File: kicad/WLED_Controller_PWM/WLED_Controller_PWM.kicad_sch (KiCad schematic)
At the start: 45 parts, among them J1 USB_C_Receptacle_USB2.0, J2 Conn_01x03, J3 Conn_01x03, J4 Conn_01x03, J6 Conn_01x02, Q1 BC847, Q2 BC847, SW1 SW_RESET, SW2 SW_BOOT, SW3 SW_Push, U1 ESP32-WROOM-32, U2 CH340C, U3 NCP1117-3.3, U4 TSSP58P38, U5 74HC14

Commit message: Add PWM Controllers
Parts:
- removed C13: 100n, Capacitor_SMD:C_0603_1608Metric_Pad1.08x0.95mm_HandSolder, symbol Device:C
- removed J2, J3, J4: Conn_01x03, GioN_Custom:TerminalBlock_WAGO_236-403_1x03_P5.00mm_45Degree, symbol Connector_Generic:Conn_01x03
- removed U5: 74HC14, Package_SO:SOIC-14_3.9x8.7mm_P1.27mm, symbol 74xx:74HC14
- added J5: Conn_01x05, GioN_Custom:TerminalBlock_WAGO_236-405_1x05_P5.00mm_45Degree, symbol Connector_Generic:Conn_01x05
- added Q3, Q4, Q5, Q6: IRFL4105PBF, Package_TO_SOT_SMD:SOT-223, symbol Transistor_FET:IRF540N
- added R13, R15, R17, R19: 100R, Resistor_SMD:R_0603_1608Metric_Pad0.98x0.95mm_HandSolder, symbol Device:R
- added R14, R16, R18, R20: 10k, Resistor_SMD:R_0603_1608Metric_Pad0.98x0.95mm_HandSolder, symbol Device:R
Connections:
- net +5V: no longer J6.1 (Pin_1)
- net GND: now also Q3.3 (S), Q4.3 (S), Q5.3 (S), Q6.3 (S), R14.1, R16.1, R18.1, R20.1
- net IO18 renamed LED_W
- net LED_W: now also R19.1
- net LED0 renamed LED_R
- net LED_R: now also R13.1
- net LED1 renamed LED_G
- net LED_G: now also R15.1
- net LED2 renamed LED_B
- net LED_B: now also R17.1
- new net: Q4.1 (G), R15.2, R16.2
- new net: Q6.1 (G), R19.2, R20.2
- new net: Q3.1 (G), R13.2, R14.2
- new net: Q5.1 (G), R17.2, R18.2
- new net: J5.4 (Pin_4), Q5.2 (D)
- new net: J5.5 (Pin_5), Q6.2 (D)
- new net: J5.2 (Pin_2), Q3.2 (D)
- new net: J5.3 (Pin_3), Q4.2 (D)
- new net +12V: J5.1 (Pin_1), J6.1 (Pin_1)

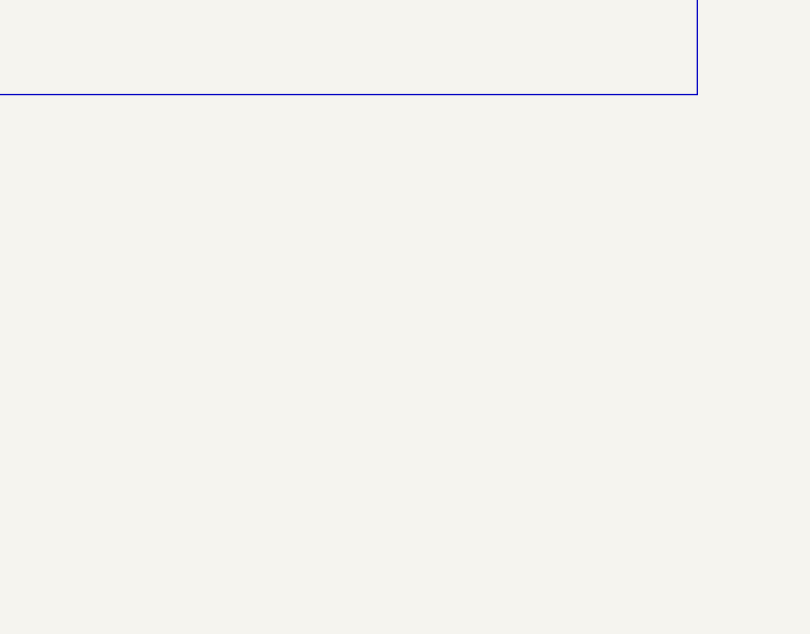
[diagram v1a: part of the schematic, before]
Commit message: add 7805
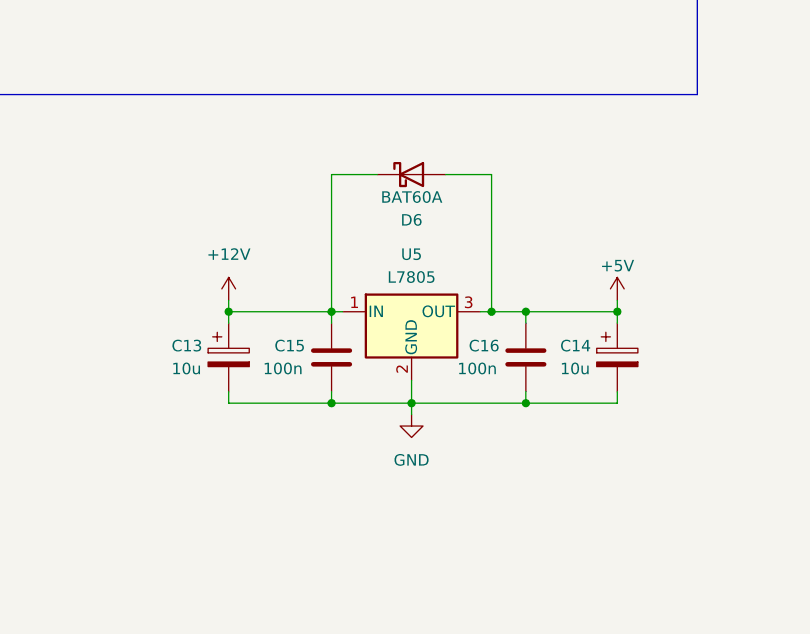
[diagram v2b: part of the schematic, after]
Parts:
- added C13, C14: 10u, Capacitor_Tantalum_SMD:CP_EIA-3216-18_Kemet-A_Pad1.58x1.35mm_HandSolder, symbol Device:C_Polarized
- added C15, C16: 100n, Capacitor_SMD:C_0603_1608Metric_Pad1.08x0.95mm_HandSolder, symbol Device:C
- added D6: BAT60A, Diode_SMD:D_SOD-323_HandSoldering, symbol Diode:BAT60A
- added U5: L7805, Package_TO_SOT_SMD:TO-252-3_TabPin2, symbol Regulator_Linear:L7805
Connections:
- net +12V: now also C13.1, C15.1, D6.1 (K), U5.1 (IN)
- net +5V: now also C14.1, C16.1, D6.2 (A), U5.3 (OUT)
- net GND: now also C13.2, C14.2, C15.2, C16.2, U5.2 (GND)

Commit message: Change to WAGO250
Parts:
- J5: footprint GioN_Custom:TerminalBlock_WAGO_236-405_1x05_P5.00mm_45Degree -> GioN_Custom:WAGO_250-205_1x05_P3.50mm
- J6: footprint GioN_Custom:TerminalBlock_WAGO_236-402_1x02_P5.00mm_45Degree -> GioN_Custom:WAGO_250-202_1x02_P3.50mm
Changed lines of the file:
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@@
       (effects (font (size 1.27 1.27)) (justify left))
     )
-    (property "Footprint" "GioN_Custom:TerminalBlock_WAGO_236-405_1x05_P5.00mm_45Degree" (at 444.5 124.46 0)
+    (property "Footprint" "GioN_Custom:WAGO_250-205_1x05_P3.50mm" (at 444.5 124.46 0)
       (effects (font (size 1.27 1.27)) hide)
     )
@@
       (effects (font (size 1.27 1.27)) (justify left))
     )
-    (property "Footprint" "GioN_Custom:TerminalBlock_WAGO_236-402_1x02_P5.00mm_45Degree" (at 125.73 134.62 0)
-      (effects (font (size 1.27 1.27)) hide)
-    )
+    (property "Footprint" "GioN_Custom:WAGO_250-202_1x02_P3.50mm" (at 125.73 134.62 0)
+      (effects (font (size 1.27 1.27)) hide)
+    )

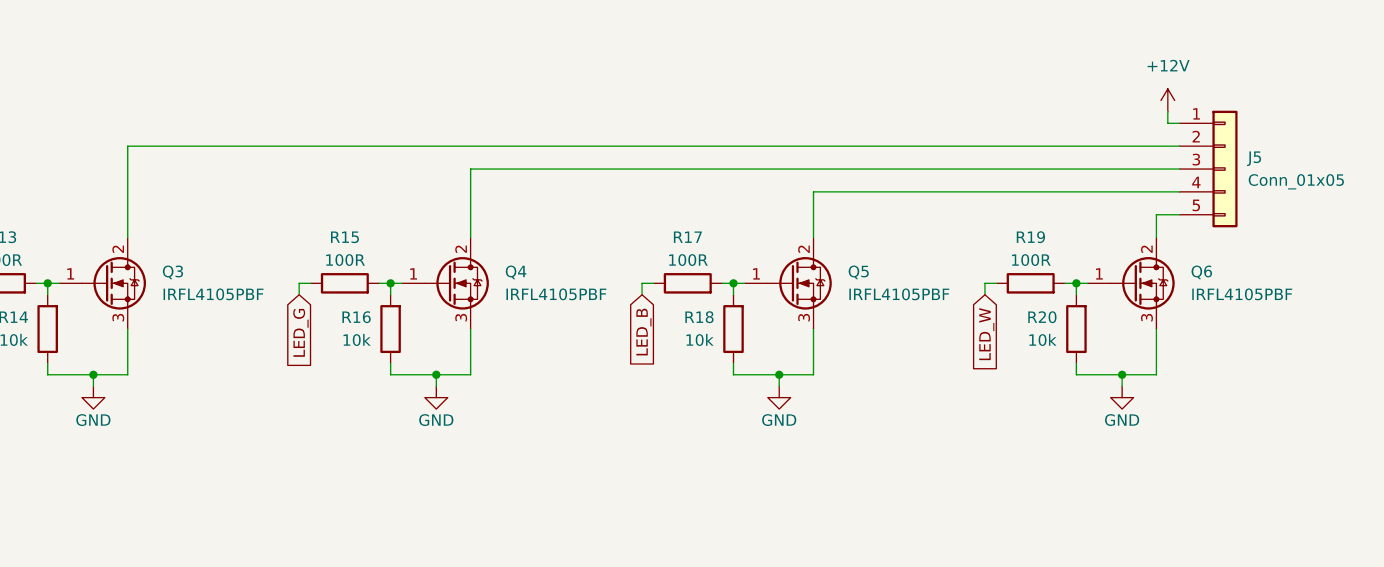
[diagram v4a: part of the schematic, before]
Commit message: change mosfet
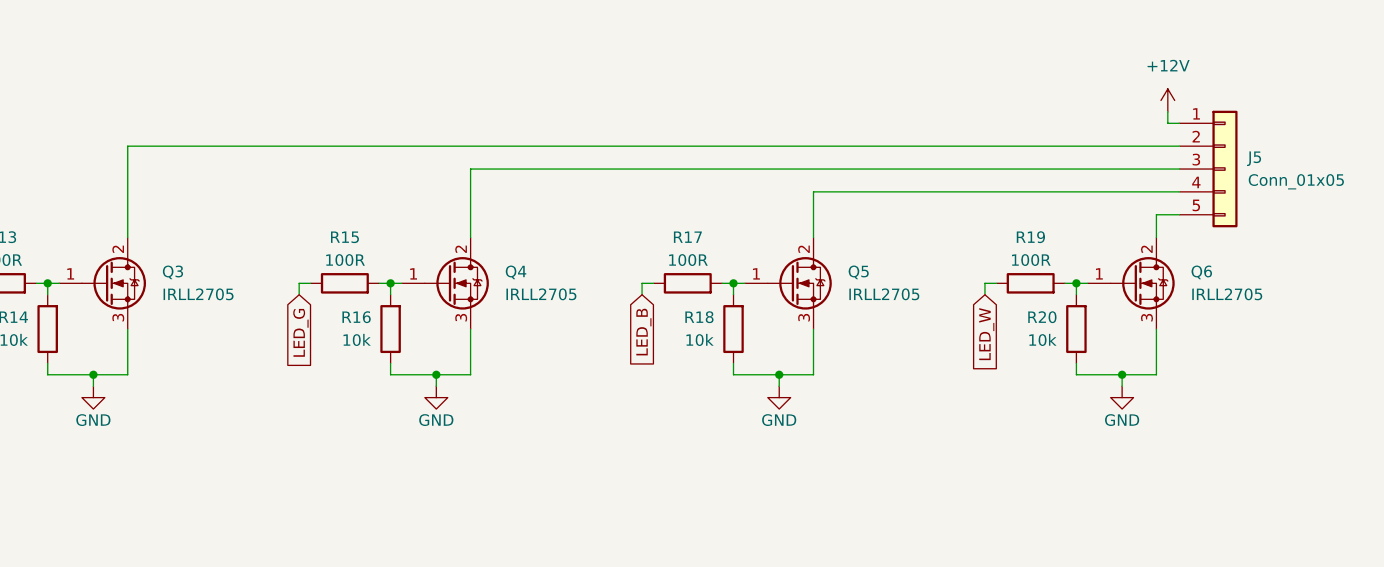
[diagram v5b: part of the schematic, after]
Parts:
- Q3, Q4, Q5, Q6: value IRFL4105PBF -> IRLL2705
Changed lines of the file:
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@@
 		(fields_autoplaced yes)
 		(property "Reference" "Q5"
-			(at 402.59 135.89 0)
-			(effects
-				(font
-					(size 1.27 1.27)
-				)
-				(justify left)
-			)
-		)
-		(property "Value" "IRFL4105PBF"
-			(at 402.59 138.43 0)
+			(at 402.59 135.8899 0)
+			(effects
+				(font
+					(size 1.27 1.27)
+				)
+				(justify left)
+			)
+		)
+		(property "Value" "IRLL2705"
+			(at 402.59 138.4299 0)
 			(effects
 				(font
@@
 		(fields_autoplaced yes)
 		(property "Reference" "Q6"
-			(at 440.69 135.89 0)
-			(effects
-				(font
-					(size 1.27 1.27)
-				)
-				(justify left)
-			)
-		)
-		(property "Value" "IRFL4105PBF"
-			(at 440.69 138.43 0)
+			(at 440.69 135.8899 0)
+			(effects
+				(font
+					(size 1.27 1.27)
+				)
+				(justify left)
+			)
+		)
+		(property "Value" "IRLL2705"
+			(at 440.69 138.4299 0)
 			(effects
 				(font
@@
 		(fields_autoplaced yes)
 		(property "Reference" "Q4"
-			(at 364.49 135.89 0)
-			(effects
-				(font
-					(size 1.27 1.27)
-				)
-				(justify left)
-			)
-		)
-		(property "Value" "IRFL4105PBF"
-			(at 364.49 138.43 0)
+			(at 364.49 135.8899 0)
+			(effects
+				(font
+					(size 1.27 1.27)
+				)
+				(justify left)
+			)
+		)
+		(property "Value" "IRLL2705"
+			(at 364.49 138.4299 0)
 			(effects
 				(font
@@
 		(fields_autoplaced yes)
 		(property "Reference" "Q3"
-			(at 326.39 135.89 0)
-			(effects
-				(font
-					(size 1.27 1.27)
-				)
-				(justify left)
-			)
-		)
-		(property "Value" "IRFL4105PBF"
-			(at 326.39 138.43 0)
-			(effects
-				(font
+			(at 326.39 135.8899 0)
+			(effects
+				(font
+					(size 1.27 1.27)
+				)
+				(justify left)
+			)
+		)
+		(property "Value" "IRLL2705"
+			(at 326.39 138.4299 0)
+			(effects
+				(font

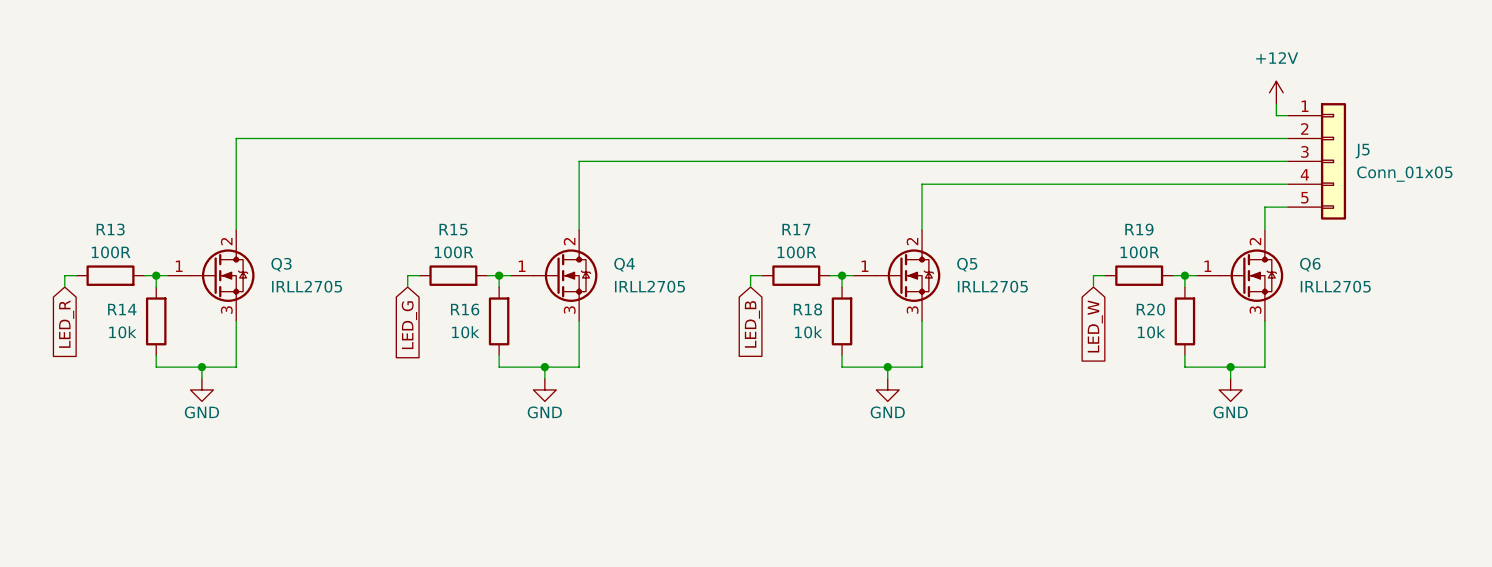
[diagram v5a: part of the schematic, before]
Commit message: Do Not Place FETS
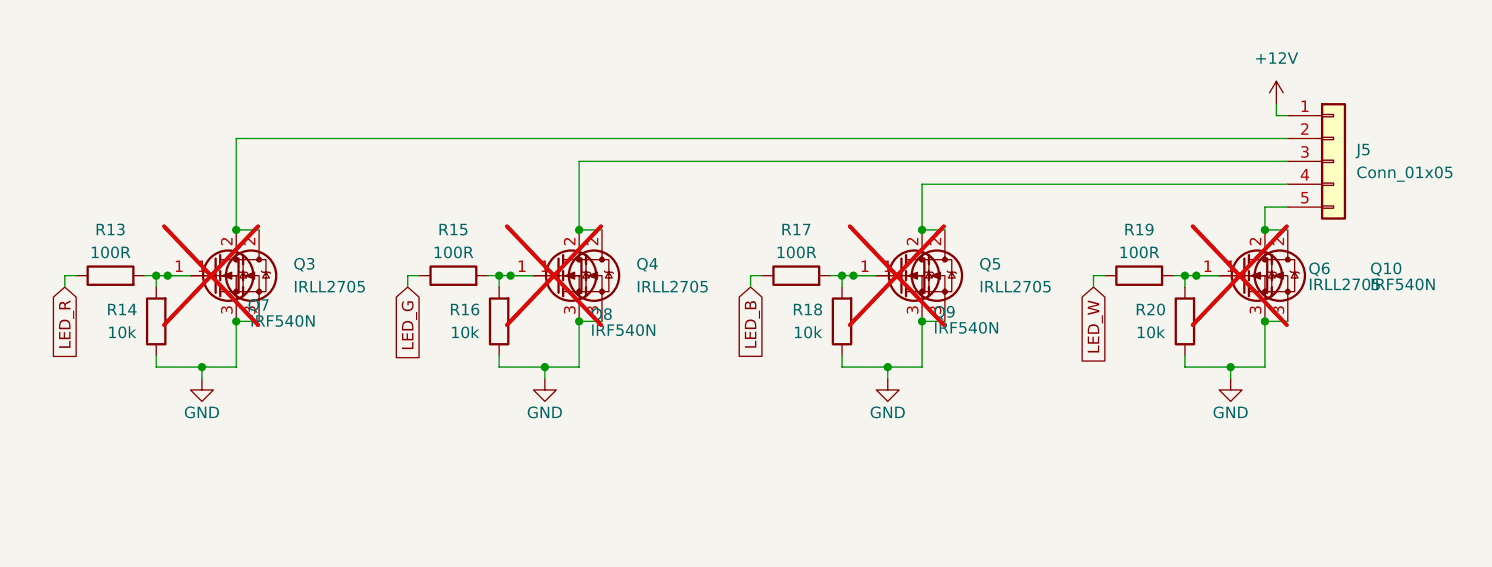
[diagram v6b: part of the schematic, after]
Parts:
- added Q10, Q7, Q8, Q9: IRF540N, Package_TO_SOT_THT:TO-220-3_Vertical, symbol Transistor_FET:IRF540N
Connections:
- net GND: now also Q10.3 (S), Q7.3 (S), Q8.3 (S), Q9.3 (S)
- net at Q4.1 (G), R15.2, R16.2: now also Q8.1 (G)
- net at Q6.1 (G), R19.2, R20.2: now also Q10.1 (G)
- net at Q3.1 (G), R13.2, R14.2: now also Q7.1 (G)
- net at Q5.1 (G), R17.2, R18.2: now also Q9.1 (G)
- net at J5.4 (Pin_4), Q5.2 (D): now also Q9.2 (D)
- net at J5.5 (Pin_5), Q6.2 (D): now also Q10.2 (D)
- net at J5.2 (Pin_2), Q3.2 (D): now also Q7.2 (D)
- net at J5.3 (Pin_3), Q4.2 (D): now also Q8.2 (D)
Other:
- moved on the sheet: Q3, Q4, Q5, Q6

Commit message: Add new PCB-Layout
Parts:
- C11: renamed from C2; LCSC (none) -> C7177
- C12: renamed from C3; LCSC (none) -> C7177
- C13: renamed from C6; LCSC (none) -> C7177
- C16: renamed from C11; LCSC (none) -> C7177
- C5: renamed from C13; LCSC (none) -> C7177
- C8: renamed from C14; LCSC (none) -> C7177
- D1: renamed from D3; LCSC (none) -> C124187
- D3: renamed from D5; now not fitted
- J1: renamed from J5; now not fitted
- J2: renamed from J1; LCSC (none) -> C2760486
- J3: renamed from J6; now not fitted
- Q10: renamed from Q6; LCSC (none) -> C151552
- Q3: LCSC (none) -> C151552
- Q5: renamed from Q4; LCSC (none) -> C151552
- Q8: renamed from Q5; LCSC (none) -> C151552
- SW1, SW2: LCSC (none) -> C843669
- SW3: now not fitted
- U1: renamed from U2; LCSC (none) -> C84681
- U2: renamed from U4; now not fitted
- U3: renamed from U5; footprint Package_TO_SOT_SMD:TO-252-3_TabPin2 -> Package_TO_SOT_SMD:TO-263-3_TabPin2; LCSC (none) -> C507146
- U4: renamed from U1; LCSC (none) -> C82899
- U5: renamed from U3; LCSC (none) -> C369933
- renumbered C5 to C1, C1 to C10, C7 to C14, C10 to C15, C8 to C2, C9 to C3, C15 to C6, C16 to C7, C12 to C9, D1 to D2, D2 to D4, D6 to D5, D4 to D6, Q7 to Q2, Q8 to Q4, Q2 to Q6, Q9 to Q7, Q10 to Q9, R9 to R1, R5 to R10, R18 to R11, R20 to R12, R1 to R13, R7 to R14, R2 to R15, R8 to R16, R4 to R17, R6 to R18, R12 to R19, R13 to R2, R11 to R20, R15 to R3, R14 to R4, R16 to R5, R10 to R6, R17 to R7, R19 to R8, R3 to R9
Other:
- note added: "12V Input"
- note added: "12V to 5V"
- note added: "5V to 3.3V"
- note added: "IR-Reciever"
- note added: "Mic."
- note added: "Output"
- note added: "Programm"
- note added: "Pushbutton"
- note added: "Serial"
- note added: "Switches"
- note removed: "Buttons"
- note removed: "PROGRAMM"
- note removed: "SERIAL"
- note removed: "SUPPLY"
- moved on the sheet: C13, C14, C15, C16, C2, C3, C5, C6, C7, C8, D2, D4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
